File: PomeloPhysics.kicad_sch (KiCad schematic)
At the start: 15 parts, among them P1 Header-Male-2.54_2x2, P2 Header-Male-2.54_2x2, U1 BroadCOM SiPM 4x4, U2 TMP116AIDRVR, U3 AT24C02D-STUM-T

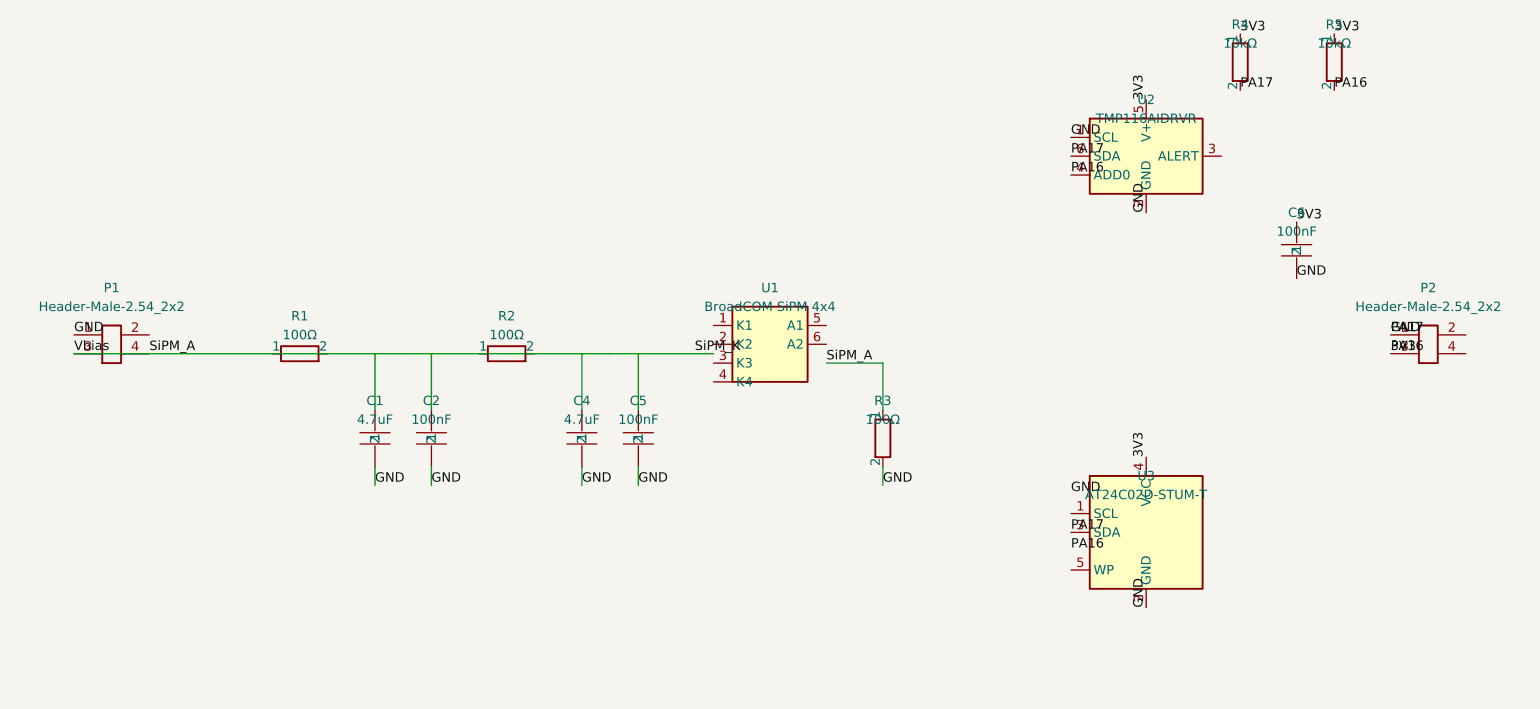
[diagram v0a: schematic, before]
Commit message: feat: Update KiCad schema to v9, rename project, and revise component symbols for library migration.
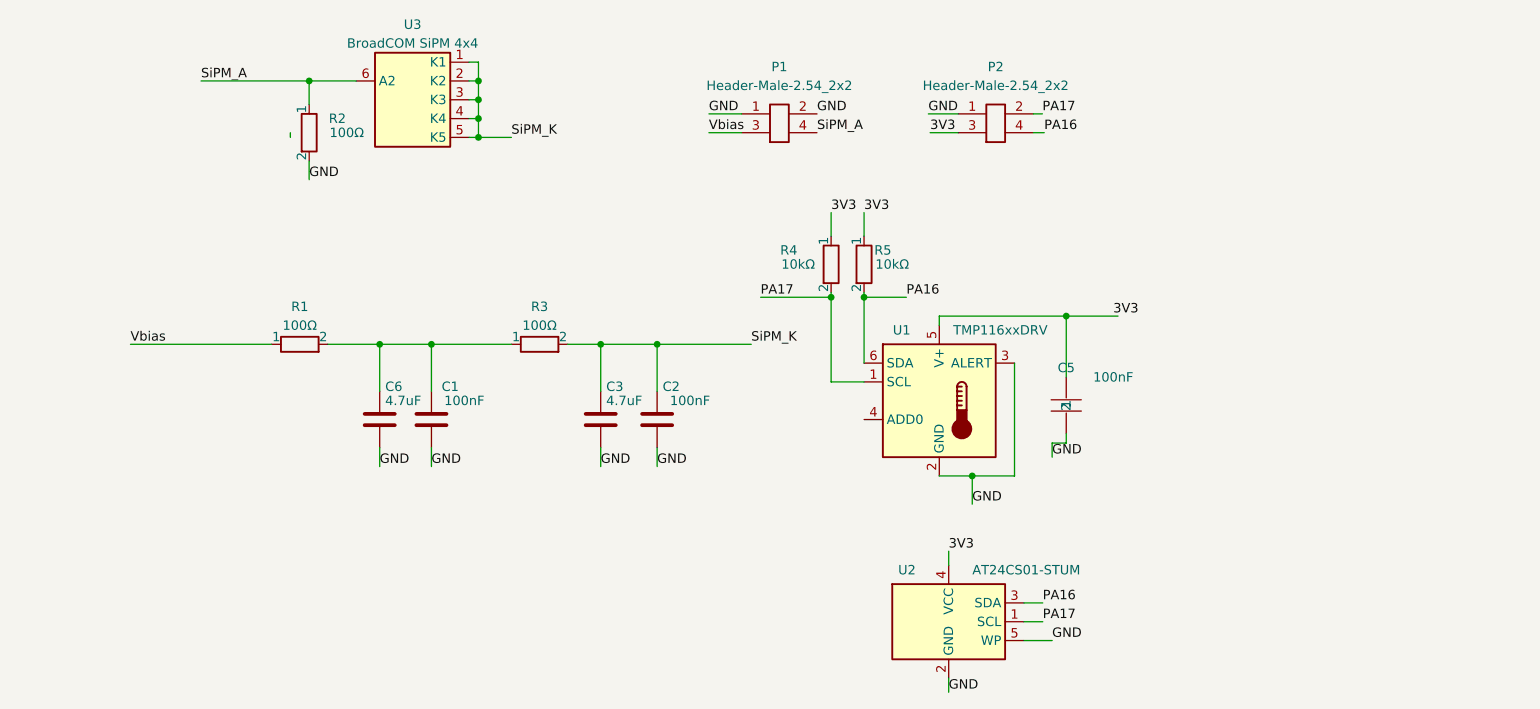
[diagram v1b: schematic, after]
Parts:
- removed C1, C4: 4.7uF, symbol C_0603
- removed C2, C6: 100nF, symbol C_0603
- removed U1: BroadCOM SiPM 4x4, symbol SiPM_4x4
- removed U2: TMP116AIDRVR, symbol TMP116
- removed U3: AT24C02D-STUM-T, symbol AT24C02
- added C1, C2: 100nF, Capacitor_SMD:C_0805_2012Metric, symbol Device:C
- added C3, C6: 4.7uF, Capacitor_SMD:C_0805_2012Metric, symbol Device:C
- added U1: TMP116xxDRV, Package_SON:WSON-6-1EP_2x2mm_P0.65mm_EP1x1.6mm, symbol Sensor_Temperature:TMP116xxDRV
- added U2: AT24CS01-STUM, Package_TO_SOT_SMD:SOT-23-5, symbol Memory_EEPROM:AT24CS01-STUM
- added U3: BroadCOM SiPM 4x4, symbol SiPM_4x4
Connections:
- net 3V3: now also C5.1, U1.5 (V+), U2.4 (VCC); no longer R5.2
- net GND: now also P1.2, R2.2, C1.2, C2.2, C3.2, C6.2, U1.2 (GND), U1.3 (ALERT), U2.2 (GND), U2.5 (WP); no longer R3.2, R4.2
- net SiPM_A: now also R2.1, U3.6 (A2); no longer P1.3, R3.1
- net PA17: now reaches P2.2
- net PA17: now also R4.2, U1.1 (SCL), U2.1 (SCL)
- net PA16: now reaches P2.4
- net PA16: now also R5.2, U1.6 (SDA), U2.3 (SDA)
- net Vbias: now reaches R1.1
- net Vbias: now also P1.3
- net at R1.2: now also R3.1, C1.1, C6.1
- new net SiPM_K: C2.1, C3.1, R3.2, U3.1 (K1), U3.2 (K2), U3.3 (K3), U3.4 (K4), U3.5 (K5)
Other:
- title: Pomelo Physics -> bGeigieScint Physics
